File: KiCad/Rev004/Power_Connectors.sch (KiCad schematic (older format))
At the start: 15 parts, among them J12 System Bus Output port, J14 ESP Interface, J15 Level_Shifter_HV, J16 Level_Shifter_LV, J18 CPU Signals, J21 Expansion port #2, J22 Expansion port #3, J5 Barrel_Jack-Connector, SW1 SW_SPDT, U13 LM3940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

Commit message: minor PCB revisions
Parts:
- added J34: Conn_01x04_Female, Connector_PinSocket_2.54mm:PinSocket_1x04_P2.54mm_Vertical, symbol Connector:Conn_01x04_Female
- added J35: Conn_01x03_Male, Connector_PinHeader_2.54mm:PinHeader_1x03_P2.54mm_Vertical, symbol Connector:Conn_01x03_Male
- added J36: Conn_01x02_Female, Connector_PinSocket_2.54mm:PinSocket_1x02_P2.54mm_Vertical, symbol Connector:Conn_01x02_Female
- J18: footprint Connector_PinSocket_2.54mm:PinSocket_2x07_P2.54mm_Vertical -> Connector_PinSocket_2.54mm:PinSocket_2x08_P2.54mm_Vertical; symbol Connector_Generic:Conn_02x07_Odd_Even -> Connector_Generic:Conn_02x08_Odd_Even
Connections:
- net +3.3V: now also J35.1 (Pin_1); no longer J14.1 (Pin_1), J14.5 (Pin_5)
- net BE: now also J18.16 (Pin_16); no longer J18.14 (Pin_14)
- net GND: now also J35.3 (Pin_3)
- net ~SO: now also J18.15 (Pin_15); no longer J18.13 (Pin_13)
- net at J16.4 (Pin_4): now also J34.3 (Pin_3)
- net at J16.5 (Pin_5): now also J34.4 (Pin_4)
- net at J15.4 (Pin_4): now also J34.1 (Pin_1)
- net at J15.5 (Pin_5): now also J34.2 (Pin_2)
- new net: J14.1 (Pin_1), J14.5 (Pin_5), J35.2 (Pin_2)
- new net ~ROM_CS: J36.1 (Pin_1)
- new net ~ROM_OE: J36.2 (Pin_2)
- no-connect marks 10 -> 8
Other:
- note added: "08/2023\nAdded breakouts for spares on level shifter"
- note added: "08/2023\nChanged JP18 to standard header size"
- note added: "08/2023\nSwitch for wireless"
- moved on the sheet: J14, J15, J16
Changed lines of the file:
@@
 Sheet 5 7
 Title "AT65C02 Hobby Computer"
-Date "2023-05-09"
+Date "2023-08-06"
 Rev "Rev004"
 Comp "This AT65C02 version by AdamT117. "
@@
 $EndDescr
 Wire Wire Line
-	3850 2000 4075 2000
-Text GLabel 4775 1700 2    50   Input ~ 0
+	2350 2775 2575 2775
+Text GLabel 4175 2475 2    50   Input ~ 0
 +3.3V
-Wire Wire Line
-	4575 1700 4775 1700
-Text GLabel 4575 1900 2    50   Input ~ 0
+Text GLabel 2350 2775 0    50   Input ~ 0
+GND
+NoConn ~ 2575 2675
+Text GLabel 2350 2475 0    50   Output ~ 0
+TxD3
+Wire Wire Line
+	3075 2775 3275 2775
+Text GLabel 2600 1125 0    50   Input ~ 0
++5V
+Text GLabel 3100 1125 2    50   Input ~ 0
 +3.3V
-Text GLabel 3850 2000 0    50   Input ~ 0
+Text GLabel 2600 1625 0    50   Input ~ 0
 GND
-NoConn ~ 4075 1900
-Text GLabel 3850 1700 0    50   Output ~ 0
+Text GLabel 3100 1625 2    50   Input ~ 0
+GND
+Text GLabel 3100 1225 2    50   Output ~ 0
 TxD3
-Wire Wire Line
-	4575 2000 4775 2000
-Text GLabel 2525 1600 0    50   Input ~ 0
-+5V
-Text GLabel 3025 1600 2    50   Input ~ 0
-+3.3V
-Text GLabel 2525 2100 0    50   Input ~ 0
-GND
-Text GLabel 3025 2100 2    50   Input ~ 0
-GND
-NoConn ~ 3025 1900
-NoConn ~ 3025 2000
-NoConn ~ 2525 1900
-NoConn ~ 2525 2000
-Text GLabel 3025 1700 2    50   Output ~ 0
-TxD3
-Text GLabel 3025 1800 2    50   Input ~ 0
+Text GLabel 3100 1325 2    50   Input ~ 0
 RxD3
 Wire Wire Line
-	4075 1700 3850 1700
-Text GLabel 4775 2000 2    50   Input ~ 0
+	2575 2475 2350 2475
+Text GLabel 3275 2775 2    50   Input ~ 0
 RxD3
 $Comp
 L AT_65C02_Computer_Rev004-rescue:Conn_02x8_Odd_Even-Connector_Generic_copy-65C02_Computer-rescue-AT_65C02_Computer-rescue-AT_65C02_Computer_Rev003_1-rescue-AT_65C02_Computer_Rev003-rescue J?
 U 1 1 639F2E0D
-P 4325 1850
+P 2825 2625
 AR Path="/5F14295C/639F2E0D" Ref="J?"  Part="1"
 AR Path="/639F2E0D" Ref="J?"  Part="1"
 AR Path="/637561AA/639F2E0D" Ref="J14"  Part="1"
-F 0 "J14" H 4325 2325 50  0000 C CNN
-F 1 "ESP Interface" H 4325 2225 50  0000 C CNN
-F 2 "Connector_PinSocket_2.54mm:PinSocket_2x04_P2.54mm_Vertical" H 4325 1850 50  0001 C CNN
-F 3 "~" H 4325 1850 50  0001 C CNN
-	1    4325 1850
+F 0 "J14" H 2825 3100 50  0000 C CNN
+F 1 "ESP Interface" H 2825 3000 50  0000 C CNN
+F 2 "Connector_PinSocket_2.54mm:PinSocket_2x04_P2.54mm_Vertical" H 2825 2625 50  0001 C CNN
+F 3 "~" H 2825 2625 50  0001 C CNN
+	1    2825 2625
 	-1   0    0    -1
 $EndComp
-Text GLabel 2525 1800 0    50   Output ~ 0
+Text GLabel 2600 1325 0    50   Output ~ 0
 RxDx
-Text GLabel 2525 1700 0    50   Input ~ 0
+Text GLabel 2600 1225 0    50   Input ~ 0
 TxDx
 Wire Wire Line
@@
 L AT_65C02_Computer_Rev004-rescue:Level_Shifter_LV-65C02_Computer-rescue-AT_65C02_Computer_Rev003_1-rescue-AT_65C02_Computer_Rev003-rescue J16
 U 1 1 6376099F
-P 2825 2100
-F 0 "J16" H 2975 2875 50  0000 C CNN
-F 1 "Level_Shifter_LV" H 3100 2750 50  0000 C CNN
-F 2 "Connector_PinSocket_2.54mm:PinSocket_1x06_P2.54mm_Vertical" H 2825 2400 50  0001 C CNN
-F 3 "" H 2825 2400 50  0001 C CNN
-	1    2825 2100
+P 2900 1625
+F 0 "J16" H 3050 2400 50  0000 C CNN
+F 1 "Level_Shifter_LV" H 3175 2275 50  0000 C CNN
+F 2 "Connector_PinSocket_2.54mm:PinSocket_1x06_P2.54mm_Vertical" H 2900 1925 50  0001 C CNN
+F 3 "" H 2900 1925 50  0001 C CNN
+	1    2900 1625
 	1    0    0    -1
 $EndComp
@@
 L AT_65C02_Computer_Rev004-rescue:Level_Shifter_HV-65C02_Computer-rescue-AT_65C02_Computer_Rev003_1-rescue-AT_65C02_Computer_Rev003-rescue J15
 U 1 1 63762084
-P 2725 2100
-F 0 "J15" H 2400 2875 50  0000 L CNN
-F 1 "Level_Shifter_HV" H 2125 2750 50  0000 L CNN
-F 2 "Connector_PinSocket_2.54mm:PinSocket_1x06_P2.54mm_Vertical" H 2725 2400 50  0001 C CNN
-F 3 "" H 2725 2400 50  0001 C CNN
-	1    2725 2100
-	1    0    0    -1
-$EndComp
-Wire Notes Line
-	1950 1200 5225 1200
-Wire Notes Line
-	5225 1200 5225 2250
-Wire Notes Line
-	5225 2250 1950 2250
-Wire Notes Line
-	1950 1200 1950 2250
+P 2800 1625
+F 0 "J15" H 2475 2400 50  0000 L CNN
+F 1 "Level_Shifter_HV" H 2200 2275 50  0000 L CNN
+F 2 "Connector_PinSocket_2.54mm:PinSocket_1x06_P2.54mm_Vertical" H 2800 1925 50  0001 C CNN
+F 3 "" H 2800 1925 50  0001 C CNN
+	1    2800 1625
+	1    0    0    -1
+$EndComp
 Wire Notes Line
 	11075 575  11075 3725
@@
 Text GLabel 10500 1450 2    50   Output ~ 0
 PWR_LED
-NoConn ~ 4575 1800
-NoConn ~ 4075 1800
+NoConn ~ 3075 2575
+NoConn ~ 2575 2575
 Text GLabel 850  7650 2    50   Input ~ 0
 a[0..15]
@@
 	1300 7650 1400 7650
 $Comp
-L Connector_Generic:Conn_02x07_Odd_Even J18
+L Connector_Generic:Conn_02x08_Odd_Even J18
 U 1 1 64939A3B
 P 8675 4675
 F 0 "J18" H 8725 5275 50  0000 C CNN
 F 1 "CPU Signals" H 8750 5200 50  0000 C CNN
-F 2 "Connector_PinSocket_2.54mm:PinSocket_2x07_P2.54mm_Vertical" H 8675 4675 50  0001 C CNN
+F 2 "Connector_PinSocket_2.54mm:PinSocket_2x08_P2.54mm_Vertical" H 8675 4675 50  0001 C CNN
 F 3 "" H 8675 4675 50  0001 C CNN
 	1    8675 4675
@@
 Text Notes 1000 3875 0    50   ~ 0
 Port is via blinky latches for display expansion (HEX board)
-Text Notes 2400 2475 0    50   ~ 0
+Text Notes 2450 1925 0    50   ~ 0
 Level shifter and ESP port
 Text Notes 6650 2775 0    50   ~ 0
@@
 Text Notes 9600 4150 0    50   ~ 0
 Capacitor C31 100uF\nminimum acording to datasheet is 33uF. \nPlease check output voltage before \nusing as less than this value results\n in 4.8v output.
-Text GLabel 8475 4975 0    50   Input ~ 0
+Text GLabel 8475 5075 0    50   Input ~ 0
 ~SO
-Text GLabel 8975 4975 2    50   Input ~ 0
+Text GLabel 8975 5075 2    50   Input ~ 0
 BE
 $Comp
@@
 Text Notes 9525 4975 0    50   ~ 0
 ROM WE should be tied \nto 5V for normal operation
+Entry Wire Line
+	2675 5425 2775 5525
+$Comp
+L Connector:Conn_01x04_Female J34
+U 1 1 64A4A140
+P 4150 1250
+F 0 "J34" H 4178 1226 50  0000 L CNN
+F 1 "Conn_01x04_Female" H 4178 1135 50  0000 L CNN
+F 2 "Connector_PinSocket_2.54mm:PinSocket_1x04_P2.54mm_Vertical" H 4150 1250 50  0001 C CNN
+F 3 "~" H 4150 1250 50  0001 C CNN
+	1    4150 1250
+	1    0    0    -1
+$EndComp
+Wire Wire Line
+	3100 1525 3650 1525
+Wire Wire Line
+	3650 1525 3650 1450
+Wire Wire Line
+	3650 1450 3950 1450
+Wire Wire Line
+	3100 1425 3575 1425
+Wire Wire Line
+	3575 1425 3575 1350
+Wire Wire Line
+	3575 1350 3950 1350
+Wire Wire Line
+	2600 1525 2075 1525
+Wire Wire Line
+	2075 1525 2075 625
+Wire Wire Line
+	2075 625  3700 625
+Wire Wire Line
+	3700 625  3700 1250
+Wire Wire Line
+	3700 1250 3950 1250
+Wire Wire Line
+	2600 1425 2150 1425
+Wire Wire Line
+	2150 1425 2150 700
+Wire Wire Line
+	2150 700  3775 700
+Wire Wire Line
+	3775 700  3775 1150
+Wire Wire Line
+	3775 1150 3950 1150
+$Comp
+L Connector:Conn_01x03_Male J35
+U 1 1 64AAAE1E
+P 3600 2100
+F 0 "J35" V 3662 2244 50  0000 L CNN
+F 1 "Conn_01x03_Male" V 3753 2244 50  0000 L CNN
+F 2 "Connector_PinHeader_2.54mm:PinHeader_1x03_P2.54mm_Vertical" H 3600 2100 50  0001 C CNN
+F 3 "~" H 3600 2100 50  0001 C CNN
+	1    3600 2100
+	0    1    1    0
+$EndComp
+Wire Wire Line
+	3700 2300 3700 2475
+Wire Wire Line
+	3700 2475 4175 2475
+Wire Wire Line
+	3600 2300 3600 2475
+Wire Wire Line
+	3075 2675 3600 2675
+Wire Wire Line
+	3075 2475 3600 2475
+Connection ~ 3600 2475
+Wire Wire Line
+	3600 2475 3600 2675
+Wire Wire Line
+	3500 2300 3350 2300
+Text GLabel 3350 2300 0    50   Input ~ 0
+GND
+Text GLabel 8550 5900 0    50   Input ~ 0
+~ROM_OE
+Text GLabel 8550 5700 0    50   Input ~ 0
+~ROM_CS
+NoConn ~ 8475 4975
+NoConn ~ 8975 4975
+$Comp
+L Connector:Conn_01x02_Female J36
+U 1 1 64B6BA7A
+P 8925 5750
+F 0 "J36" H 8953 5726 50  0000 L CNN
+F 1 "Conn_01x02_Female" H 8953 5635 50  0000 L CNN
+F 2 "Connector_PinSocket_2.54mm:PinSocket_1x02_P2.54mm_Vertical" H 8925 5750 50  0001 C CNN
+F 3 "~" H 8925 5750 50  0001 C CNN
+	1    8925 5750
+	1    0    0    -1
+$EndComp
+Wire Wire Line
+	8550 5700 8725 5700
+Wire Wire Line
+	8725 5700 8725 5750
+Wire Wire Line
+	8550 5900 8725 5900
+Wire Wire Line
+	8725 5900 8725 5850
 Wire Bus Line
 	2775 5225 2775 5800
@@
 Wire Bus Line
 	750  6100 750  7650
-Entry Wire Line
-	2675 5425 2775 5525
+Text Notes 4850 2375 0    50   ~ 0
+08/2023\nSwitch for wireless
+Text Notes 4675 1000 0    50   ~ 0
+08/2023\nAdded breakouts for spares on level shifter
+Text Notes 9575 4575 0    50   ~ 0
+08/2023\nChanged JP18 to standard header size
 $EndSCHEMATC

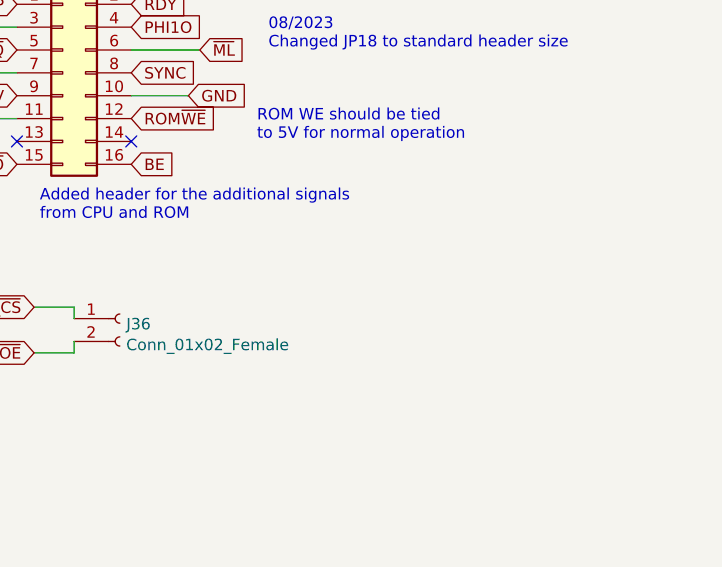
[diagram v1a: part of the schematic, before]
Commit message: Jumper explanation added
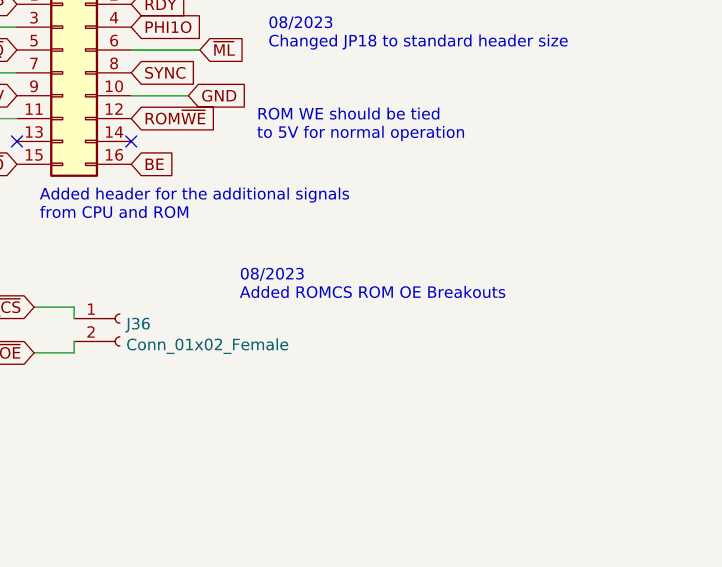
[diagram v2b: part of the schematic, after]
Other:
- note added: "08/2023\nAdded ROMCS ROM OE Breakouts"
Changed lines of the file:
@@
 Wire Wire Line
 	8725 5900 8725 5850
+Text Notes 4850 2375 0    50   ~ 0
+08/2023\nSwitch for wireless
+Text Notes 4675 1000 0    50   ~ 0
+08/2023\nAdded breakouts for spares on level shifter
+Text Notes 9575 4575 0    50   ~ 0
+08/2023\nChanged JP18 to standard header size
 Wire Bus Line
 	2775 5225 2775 5800
@@
 Wire Bus Line
 	750  6100 750  7650
-Text Notes 4850 2375 0    50   ~ 0
-08/2023\nSwitch for wireless
-Text Notes 4675 1000 0    50   ~ 0
-08/2023\nAdded breakouts for spares on level shifter
-Text Notes 9575 4575 0    50   ~ 0
-08/2023\nChanged JP18 to standard header size
+Text Notes 9450 5675 0    50   ~ 0
+08/2023\nAdded ROMCS ROM OE Breakouts
 $EndSCHEMATC
